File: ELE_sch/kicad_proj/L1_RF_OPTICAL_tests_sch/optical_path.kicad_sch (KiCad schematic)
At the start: 8 parts

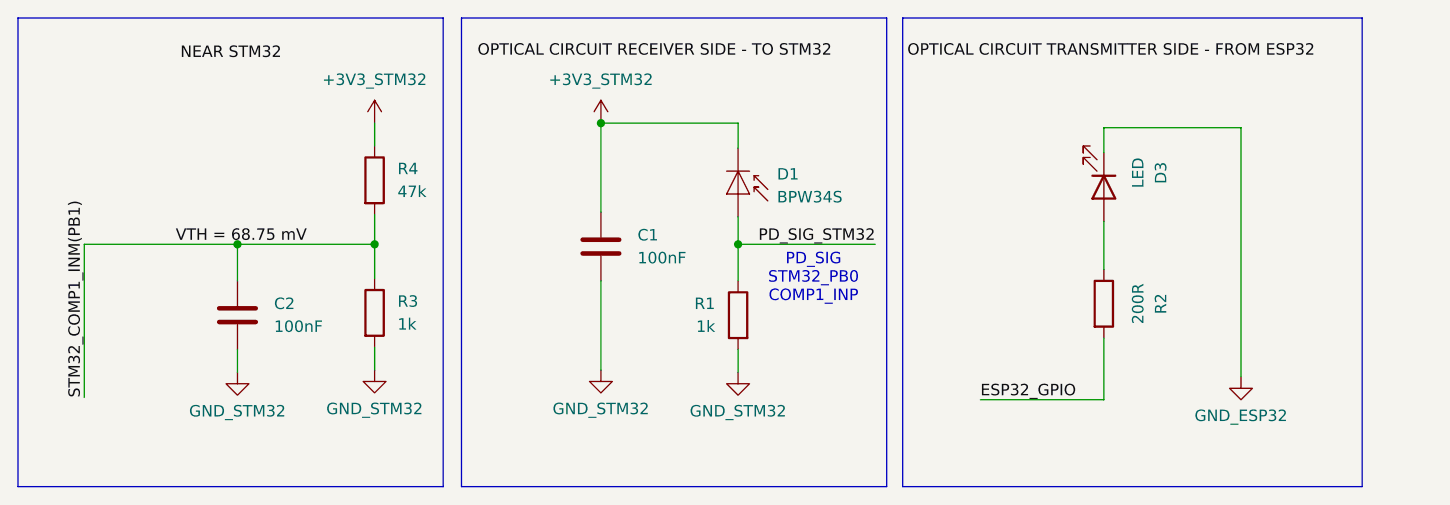
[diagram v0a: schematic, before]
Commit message: update of pinouts, schematics
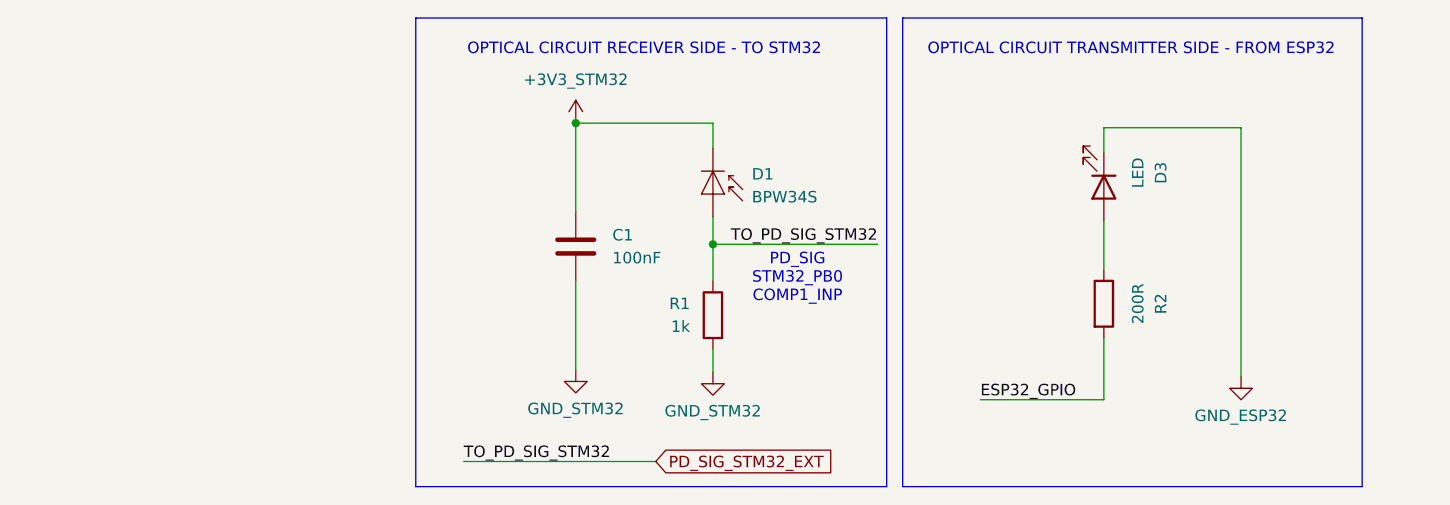
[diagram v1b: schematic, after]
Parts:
- removed C2: 100nF, symbol Device:C
- removed R3: 1k, symbol Device:R
- removed R4: 47k, symbol Device:R
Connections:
- net PD_SIG_STM32 renamed PD_SIG_STM32_EXT
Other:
- note added: "OPTICAL CIRCUIT RECEIVER SIDE - TO STM32"
- note added: "OPTICAL CIRCUIT TRANSMITTER SIDE - FROM ESP32"
- moved on the sheet: C1, D1, R1

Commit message: Update optical_path.kicad_sch
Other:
- note added: "PD_SIG STM32_PE9 COMP2_INP"
- note removed: "PD_SIG STM32_PB0 COMP1_INP"
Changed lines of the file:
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@@
 		)
 	)
-	(text "PD_SIG\nSTM32_PB0\nCOMP1_INP"
+	(text "PD_SIG\nSTM32_PE9\nCOMP2_INP"
 		(exclude_from_sim no)
 		(at 148.844 110.998 0)
